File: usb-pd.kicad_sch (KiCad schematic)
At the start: 65 parts, among them J3 USB-C_GCT_USB4105-GF-A, Q6 SQS401EN-T1_BE3, Q8 BSS138-7-F, U5 CYPD3177-24LQXQ, U9 SIC477ED-T1-GE3

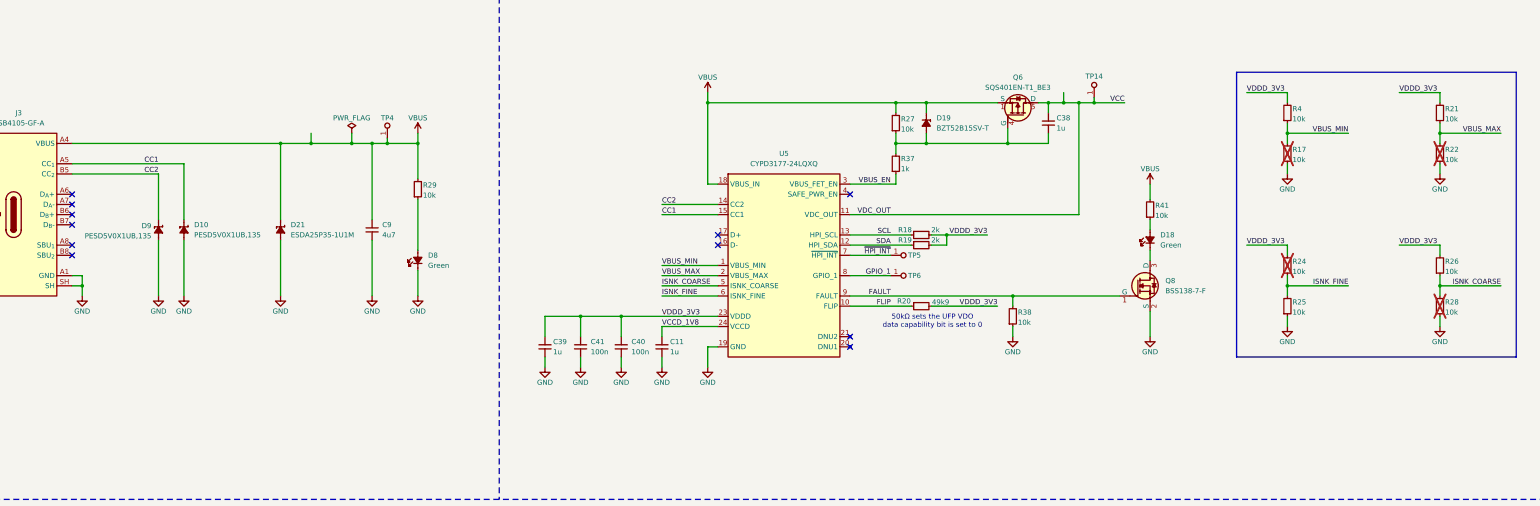
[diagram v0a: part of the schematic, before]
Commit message: [#79426] Small USB-PD improvements
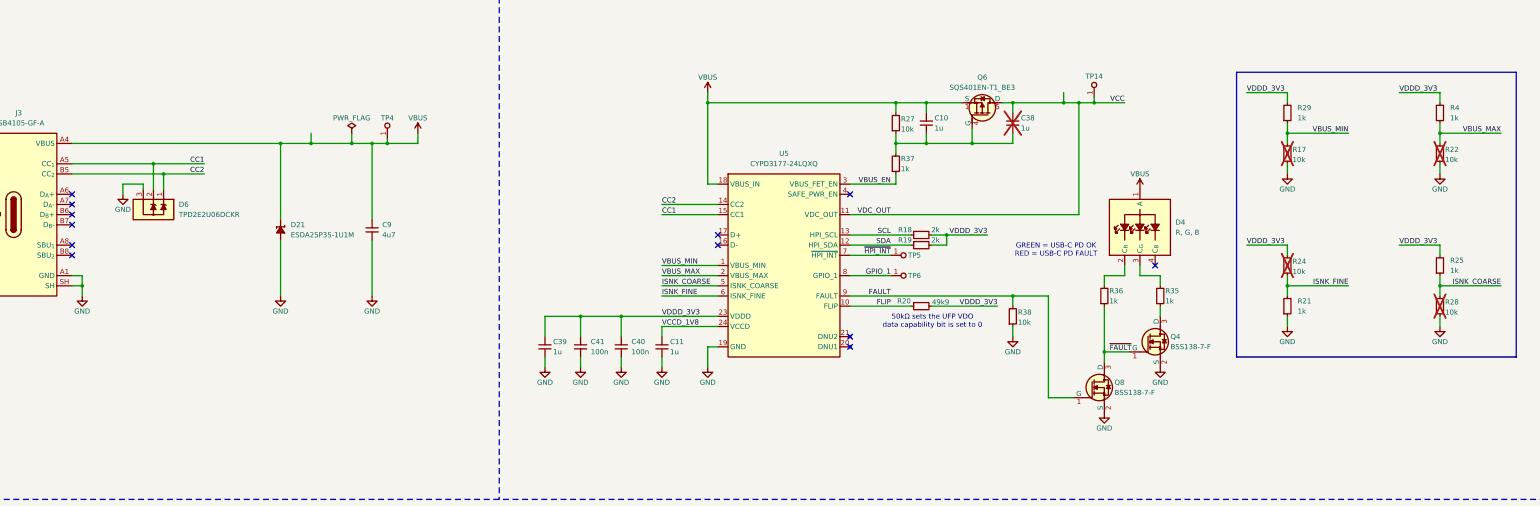
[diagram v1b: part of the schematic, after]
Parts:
- removed D10, D9: PESD5V0X1UB, antmicro-footprints:SOD-523, symbol antmicroTVSDiodes:PESD5V0X1UB
- removed D18, D8: LED_G_0603_LTST-C190GKT, antmicro-footprints:LED_0603_1608Metric_G, symbol antmicroLEDIndicationDiscrete:LED_G_0603_LTST-C190GKT
- removed D19: BZT52B15SV-T, antmicro-footprints:D_SOD-323, symbol antmicroDiodesZenerSingle:BZT52B15SV-T
- removed R21, R25, R26, R29, R4, R41: R_10k_0402, antmicro-footprints:R_0402_1005Metric, symbol antmicroResistors0402:R_10k_0402
- added C10: C_1u_25V_0402, antmicro-footprints:C_0402_1005Metric, symbol antmicroCapacitors0402:C_1u_25V_0402
- added D4: LED_RGB_0404_150044M155260, antmicro-footprints:LED_0404_1010Metric_RGB, symbol antmicroLEDIndicationDiscrete:LED_RGB_0404_150044M155260
- added D6: TPD2E2U06_SC70, antmicro-footprints:SC70-3, symbol antmicroTVSDiodes:TPD2E2U06_SC70
- added Q4: BSS138-7-F, antmicro-footprints:SOT-23-3, symbol antmicroTransistorsFETsMOSFETsSingle:BSS138-7-F
- added R21, R25, R29, R35, R36, R4: R_1k_0402, antmicro-footprints:R_0402_1005Metric, symbol antmicroResistors0402:R_1k_0402
- C38: now not fitted
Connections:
- net CC1: now also D6.2
- net CC2: now also D6.1
- net GND: now also D6.3, Q4.2 (S), R21.1
- net ISNK_COARSE: now also R25.1
- net ISNK_FINE: now also R21.2
- net VBUS: now also C10.2, D4.1 (A)
- net VBUS_MAX: now also R4.1
- net VBUS_MIN: now also R29.1
- net VDDD_3V3: now also R25.2, R29.2, R4.2
- net at C38.1, Q6.4 (G), R27.1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: now also C10.1
- net ~{FAULT}: now reaches Q8.3 (D)
- net ~{FAULT}: now also Q4.1 (G), R36.1
- new net: Q4.3 (D), R35.1
- new net: D4.3 (C_{G}), R35.2
- new net: D4.2 (C_{R}), R36.2
- no-connect marks 14 -> 15
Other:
- note added: "GREEN = USB-C PD OK RED = USB-C PD FAULT"
- moved on the sheet: Q6, Q8

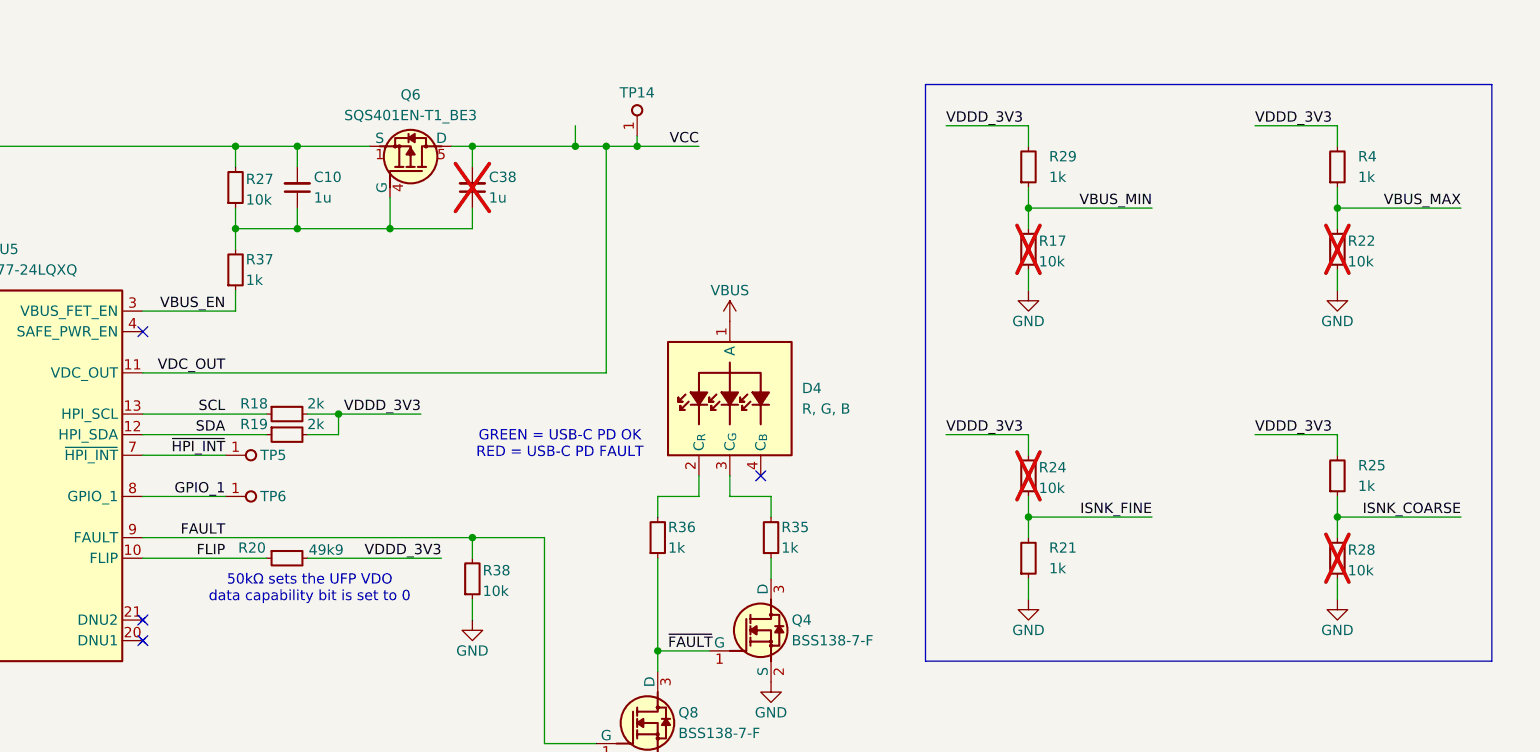
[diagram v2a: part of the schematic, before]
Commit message: [#79426] Minor USB-C PD schematic fixes
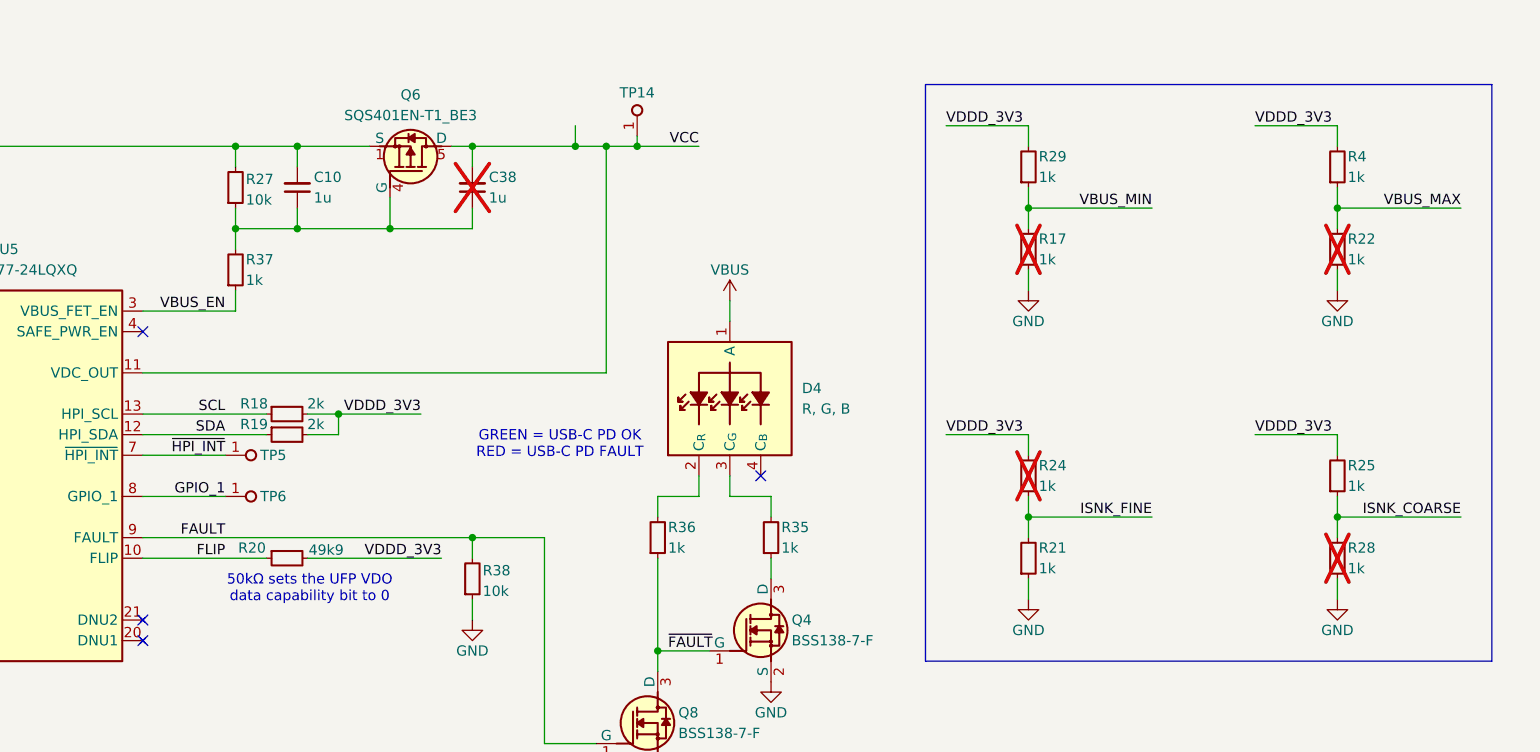
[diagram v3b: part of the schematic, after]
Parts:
- removed R17, R22, R24, R28: R_10k_0402, antmicro-footprints:R_0402_1005Metric, symbol antmicroResistors0402:R_10k_0402
- added R17, R22, R24, R28: R_1k_0402, antmicro-footprints:R_0402_1005Metric, symbol antmicroResistors0402:R_1k_0402
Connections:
- net GND: now also R17.1, R22.1, R28.1
- net ISNK_COARSE: now also R28.2
- net ISNK_FINE: now also R24.1
- net VBUS_MAX: now also R22.2
- net VBUS_MIN: now also R17.2
- net VDDD_3V3: now also R24.2
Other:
- note added: "50kΩ sets the UFP VDO data capability bit to 0"
- note removed: "50kΩ sets the UFP VDO data capability bit is set to 0"

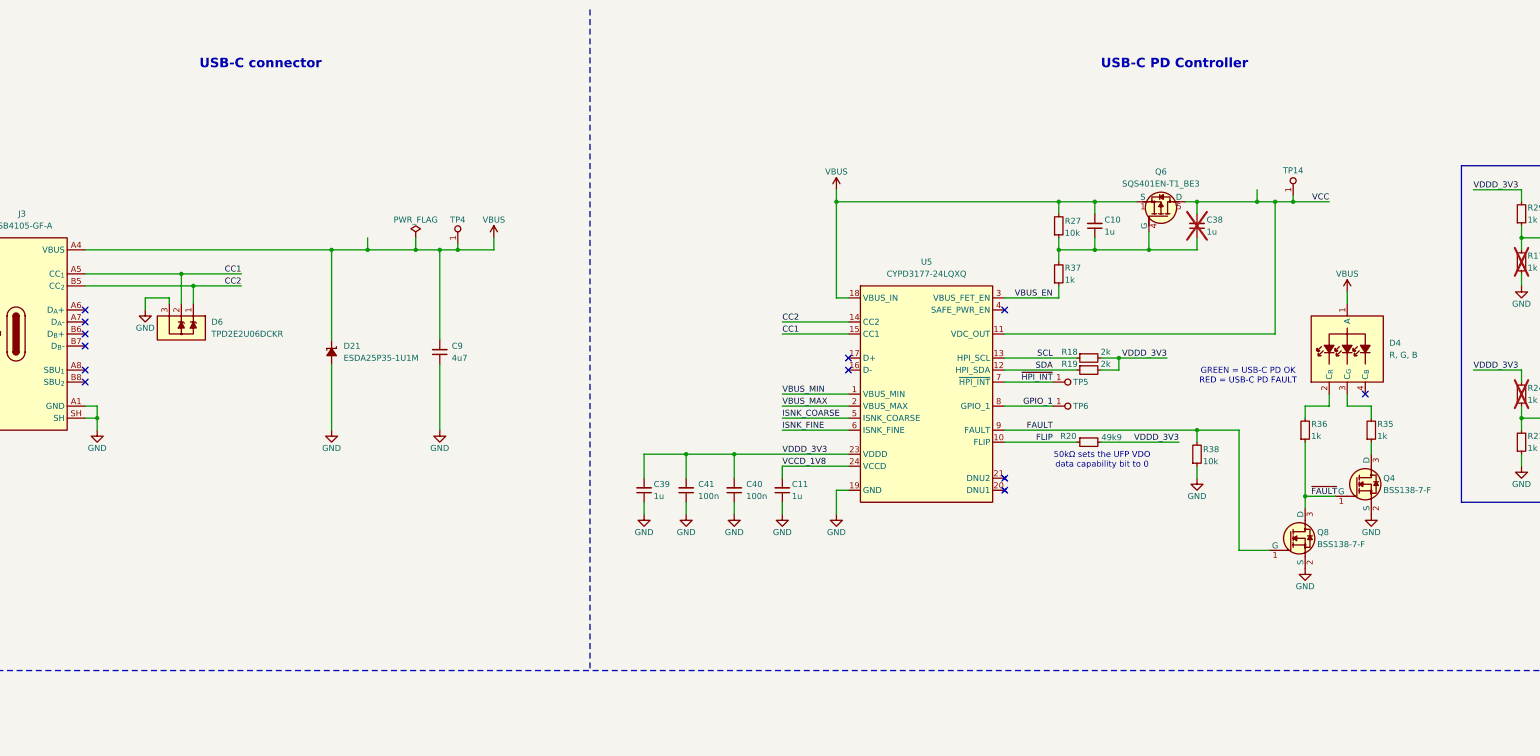
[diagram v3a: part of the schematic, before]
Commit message: [#79426] Fix USB-PD fault LED to prevent excessive MOSFET Vgs
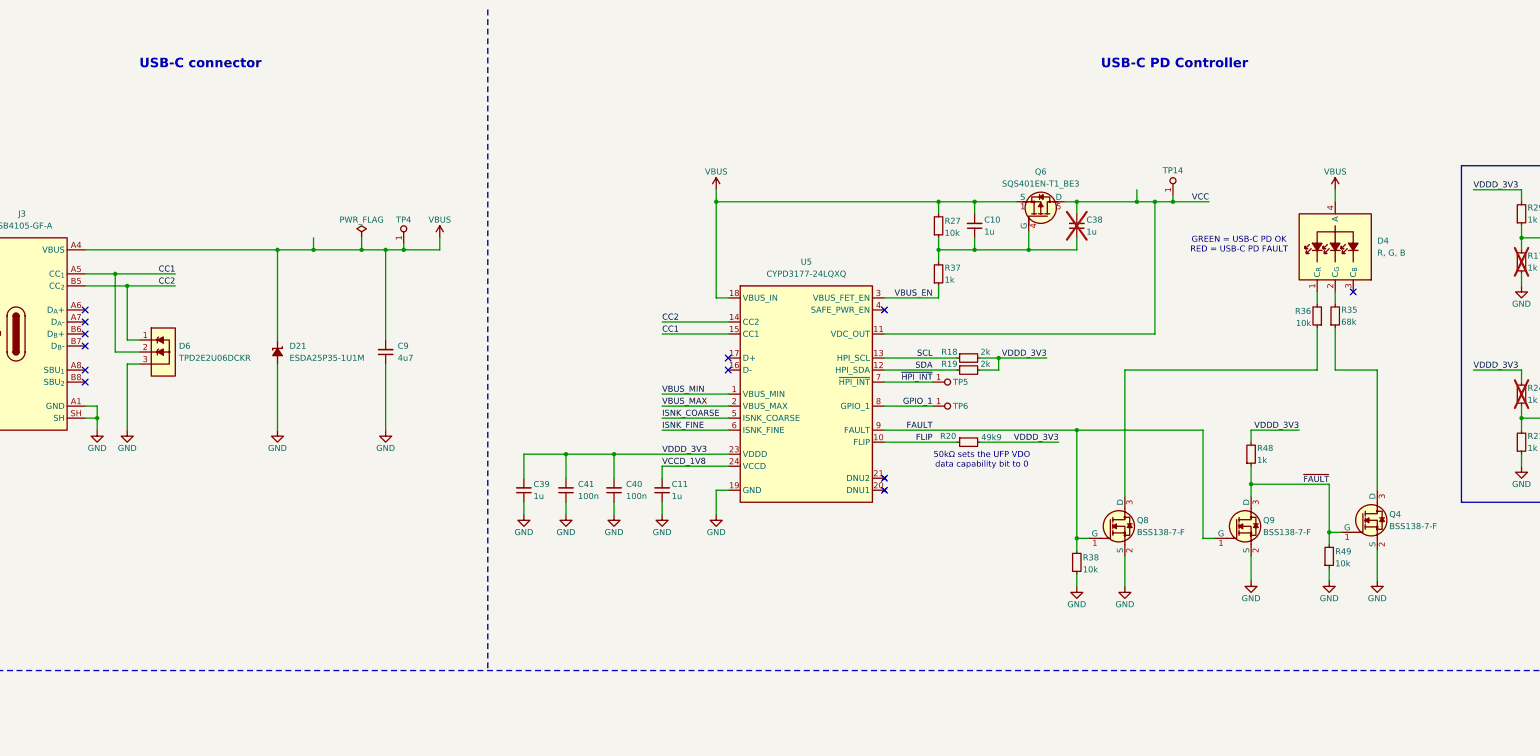
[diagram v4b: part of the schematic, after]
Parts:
- removed D4: LED_RGB_0404_150044M155260, antmicro-footprints:LED_0404_1010Metric_RGB, symbol antmicroLEDIndicationDiscrete:LED_RGB_0404_150044M155260
- removed R35, R36: R_1k_0402, antmicro-footprints:R_0402_1005Metric, symbol antmicroResistors0402:R_1k_0402
- added D4: LED_RGB_PLCC4_ASMB_MTB1_0A3A2, antmicro-footprints:PLCC4_3.2x2.8mm, symbol antmicroLEDIndicationDiscrete:LED_RGB_PLCC4_ASMB_MTB1_0A3A2
- added Q9: BSS138-7-F, antmicro-footprints:SOT-23-3, symbol antmicroTransistorsFETsMOSFETsSingle:BSS138-7-F
- added R35: R_68k_0402, antmicro-footprints:R_0402_1005Metric, symbol antmicroResistors0402:R_68k_0402
- added R36, R49: R_10k_0402, antmicro-footprints:R_0402_1005Metric, symbol antmicroResistors0402:R_10k_0402
- added R48: R_1k_0402, antmicro-footprints:R_0402_1005Metric, symbol antmicroResistors0402:R_1k_0402
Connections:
- net FAULT: now also Q9.1 (G)
- net GND: now also Q9.2 (S), R49.1
- net VBUS: now also D4.4 (A)
- net VDDD_3V3: now also R48.2
- net ~{FAULT}: now also Q9.3 (D), R48.1, R49.2; no longer Q8.3 (D)
- net at Q4.3 (D): now also R35.1
- new net: Q8.3 (D), R36.1
- new net: D4.1 (C_{R}), R36.2
- new net: D4.2 (C_{G}), R35.2
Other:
- moved on the sheet: C10, C11, C38, C39, C40, C41, C9, D21, D6, Q4, Q6, Q8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

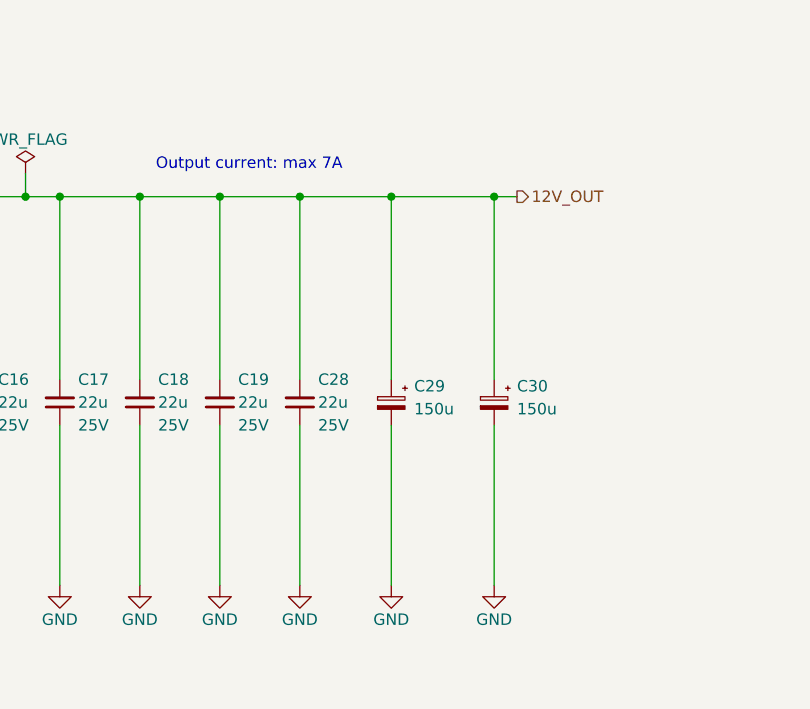
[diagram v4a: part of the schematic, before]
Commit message: [#79262] Route high speed and power
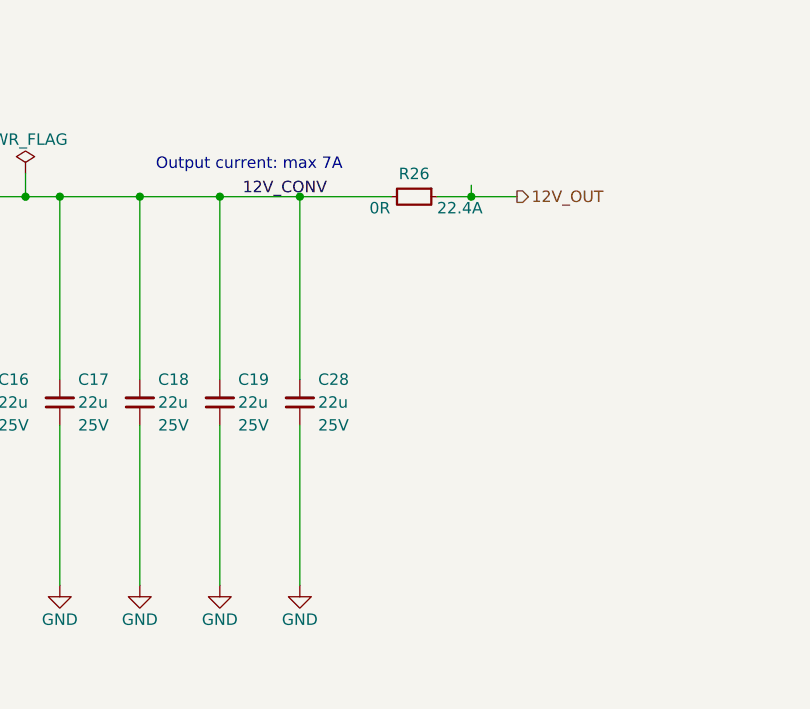
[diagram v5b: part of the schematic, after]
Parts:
- removed C29, C30: C_Pol_150u_30V_Vishay-T59-EE, antmicro-footprints:C_Pol_Vishay-T59-EE, symbol antmicroCapacitorspol:C_Pol_150u_30V_Vishay-T59-EE
- added R26: R_0R_22.4A_0603, antmicro-footprints:R_0603_1608Metric, symbol antmicroResistors0603:R_0R_22.4A_0603
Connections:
- net 12V_OUT: now also R26.1; no longer C16.2, C17.2, C18.2, C19.2, C28.2, C31.2, L2.2, R40.2, TP13.1, U9.20 (V_{SNS})
- new net 12V_CONV: C16.2, C17.2, C18.2, C19.2, C28.2, C31.2, L2.2, R26.2, R40.2, TP13.1, U9.20 (V_{SNS})

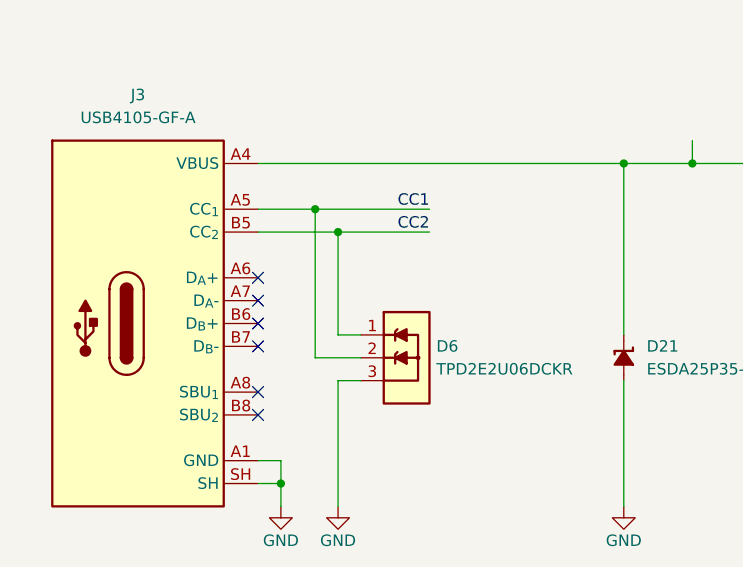
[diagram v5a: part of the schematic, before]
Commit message: [#79262] Connect all the signals
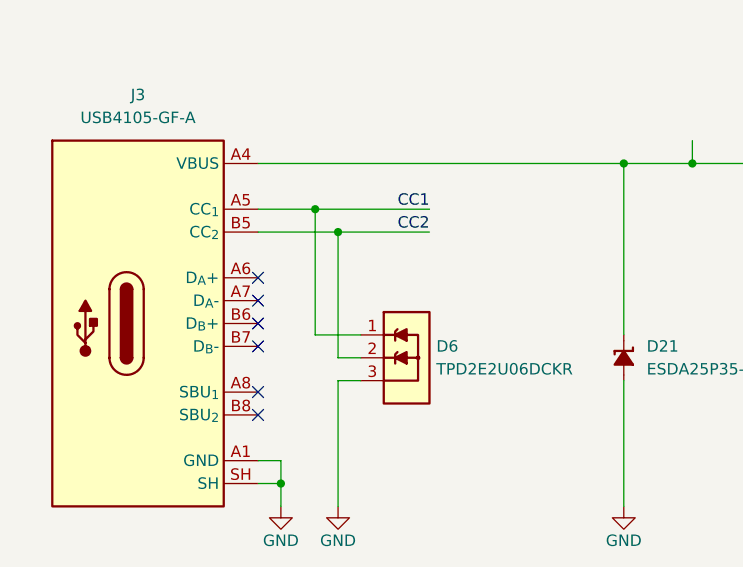
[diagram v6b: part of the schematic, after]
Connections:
- net CC1: now also D6.1; no longer D6.2
- net CC2: now also D6.2; no longer D6.1
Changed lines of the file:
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@@
+	(wire
+		(pts
+			(xy 48.26 85.09) (xy 50.8 85.09)
+		)
+		(stroke
+			(width 0)
+			(type default)
+		)
+	)
 	(wire
 		(pts
@@
 	(wire
 		(pts
+			(xy 48.26 71.12) (xy 48.26 85.09)
+		)
+		(stroke
+			(width 0)
+			(type default)
+		)
+	)
+	(wire
+		(pts
 			(xy 107.95 210.82) (xy 107.95 228.6)
 		)
@@
 	(wire
 		(pts
-			(xy 45.72 68.58) (xy 45.72 85.09)
+			(xy 45.72 68.58) (xy 45.72 82.55)
 		)
 		(stroke
@@
 	(wire
 		(pts
-			(xy 48.26 82.55) (xy 48.26 71.12)
-		)
-		(stroke
-			(width 0)
-			(type default)
-		)
-	)
-	(wire
-		(pts
 			(xy 204.47 226.06) (xy 207.01 226.06)
 		)
@@
 	(wire
 		(pts
-			(xy 48.26 82.55) (xy 50.8 82.55)
-		)
-		(stroke
-			(width 0)
-			(type default)
-		)
-	)
-	(wire
-		(pts
 			(xy 312.42 133.35) (xy 312.42 127)
 		)
@@
 	(wire
 		(pts
+			(xy 45.72 82.55) (xy 50.8 82.55)
+		)
+		(stroke
+			(width 0)
+			(type default)
+		)
+	)
+	(wire
+		(pts
 			(xy 140.97 116.84) (xy 140.97 119.38)
 		)
@@
 		)
 		(stroke
-			(width 0)
-			(type default)
-		)
-	)
-	(wire
-		(pts
-			(xy 50.8 85.09) (xy 45.72 85.09)
-		)
-		(stroke
